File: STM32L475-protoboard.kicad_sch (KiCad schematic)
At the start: 69 parts, among them J1 USB_HEADER, J10 Conn_01x02_Male, J11 SD_Card, J2 USB_B_Micro, J3 DCin, J4 STLINK, J5 W5500_ETHERNET, J6 STLINK2, J7 BOOT_MODE, J8 Conn_02x20_Odd_Even, J9 Conn_01x02_Male, SW1 RESET, U1 SRV05-4, U2 AMS1117-3.3, U3 STM32L475RCTx, Y1 16 MHz, Y2 32.768k

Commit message: some more pins
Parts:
- added C20, C21: 12p, Capacitor_SMD:C_0603_1608Metric, symbol Device:C_Small
- added J10: GNDPAD, Connector_Wire:SolderWirePad_1x01_SMD_1x2mm, symbol Connector:Conn_01x01_Male
- added J8: PAD_PA9_USART1_TX, Connector_Wire:SolderWirePad_1x01_SMD_1x2mm, symbol Connector:Conn_01x01_Male
- added J9: PAD_PA10_USART1_RX, Connector_Wire:SolderWirePad_1x01_SMD_1x2mm, symbol Connector:Conn_01x01_Male
- renumbered C11 to C10, C12 to C11, C13 to C12, C7 to C13, C19 to C18, C18 to C19, C20 to C22, C21 to C23, C22 to C24, C8 to C7, C9 to C8, C10 to C9, J9 to J11, J10 to J12, J8 to J13, J11 to J14, R3 to R2, R4 to R3, R5 to R4, R6 to R5, R2 to R6
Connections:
- net +3V3: now also J13.7 (Pin_7)
- net GND: now also C20.1, C21.1, J10.1 (Pin_1)
- net LED_USR1: now also J13.39 (Pin_39); no longer J13.37 (Pin_37)
- net LED_USR2: now also J13.37 (Pin_37); no longer J13.39 (Pin_39)
- net PA2: now reaches U3.16 (PA2)
- net PA2: now also J13.35 (Pin_35)
- net PA3: now reaches U3.17 (PA3)
- net PA3: now also J13.33 (Pin_33)
- net PA4: now reaches U3.20 (PA4)
- net PA4: now also J13.31 (Pin_31)
- net PA5: now reaches U3.21 (PA5)
- net PA5: now also J13.29 (Pin_29)
- net PA6: now reaches U3.22 (PA6)
- net PA6: now also J13.27 (Pin_27), C20.2
- net PA7: now reaches U3.23 (PA7)
- net PA7: now also J13.25 (Pin_25), C21.2
- net PA9: now reaches U3.42 (PA9)
- net PA9: now also J8.1 (Pin_1)
- net USB_ID renamed PA10
- net PA10: now also J9.1 (Pin_1)
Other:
- moved on the sheet: J13

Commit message: texts
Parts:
- C20, C21: value 12p -> DNP; footprint Capacitor_SMD:C_0603_1608Metric -> Capacitor_SMD:C_0805_2012Metric_Pad1.18x1.45mm_HandSolder
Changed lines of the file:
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@@
     (in_bom yes) (on_board yes)
     (property "Reference" "C21" (id 0) (at 231.14 62.23 90))
-    (property "Value" "12p" (id 1) (at 233.68 62.23 90))
-    (property "Footprint" "Capacitor_SMD:C_0603_1608Metric" (id 2) (at 228.6 62.23 0)
+    (property "Value" "DNP" (id 1) (at 233.68 62.23 90))
+    (property "Footprint" "Capacitor_SMD:C_0805_2012Metric_Pad1.18x1.45mm_HandSolder" (id 2) (at 228.6 62.23 0)
       (effects (font (size 1.27 1.27)) hide)
     )
@@
     (in_bom yes) (on_board yes)
     (property "Reference" "C20" (id 0) (at 231.14 52.07 90))
-    (property "Value" "12p" (id 1) (at 233.68 52.07 90))
-    (property "Footprint" "Capacitor_SMD:C_0603_1608Metric" (id 2) (at 228.6 52.07 0)
+    (property "Value" "DNP" (id 1) (at 233.68 52.07 90))
+    (property "Footprint" "Capacitor_SMD:C_0805_2012Metric_Pad1.18x1.45mm_HandSolder" (id 2) (at 228.6 52.07 0)
       (effects (font (size 1.27 1.27)) hide)
     )
@@
     )
     (path "/e06a59e6-3afe-4857-8998-a5946749a3af"
-      (reference "C20") (unit 1) (value "12p") (footprint "Capacitor_SMD:C_0603_1608Metric")
+      (reference "C20") (unit 1) (value "DNP") (footprint "Capacitor_SMD:C_0805_2012Metric_Pad1.18x1.45mm_HandSolder")
     )
     (path "/097e26fe-f01a-4812-ac65-b308a8eb46ac"
-      (reference "C21") (unit 1) (value "12p") (footprint "Capacitor_SMD:C_0603_1608Metric")
+      (reference "C21") (unit 1) (value "DNP") (footprint "Capacitor_SMD:C_0805_2012Metric_Pad1.18x1.45mm_HandSolder")
     )
     (path "/bf7728b2-c0d3-4e01-ba3c-30550cdcc695"

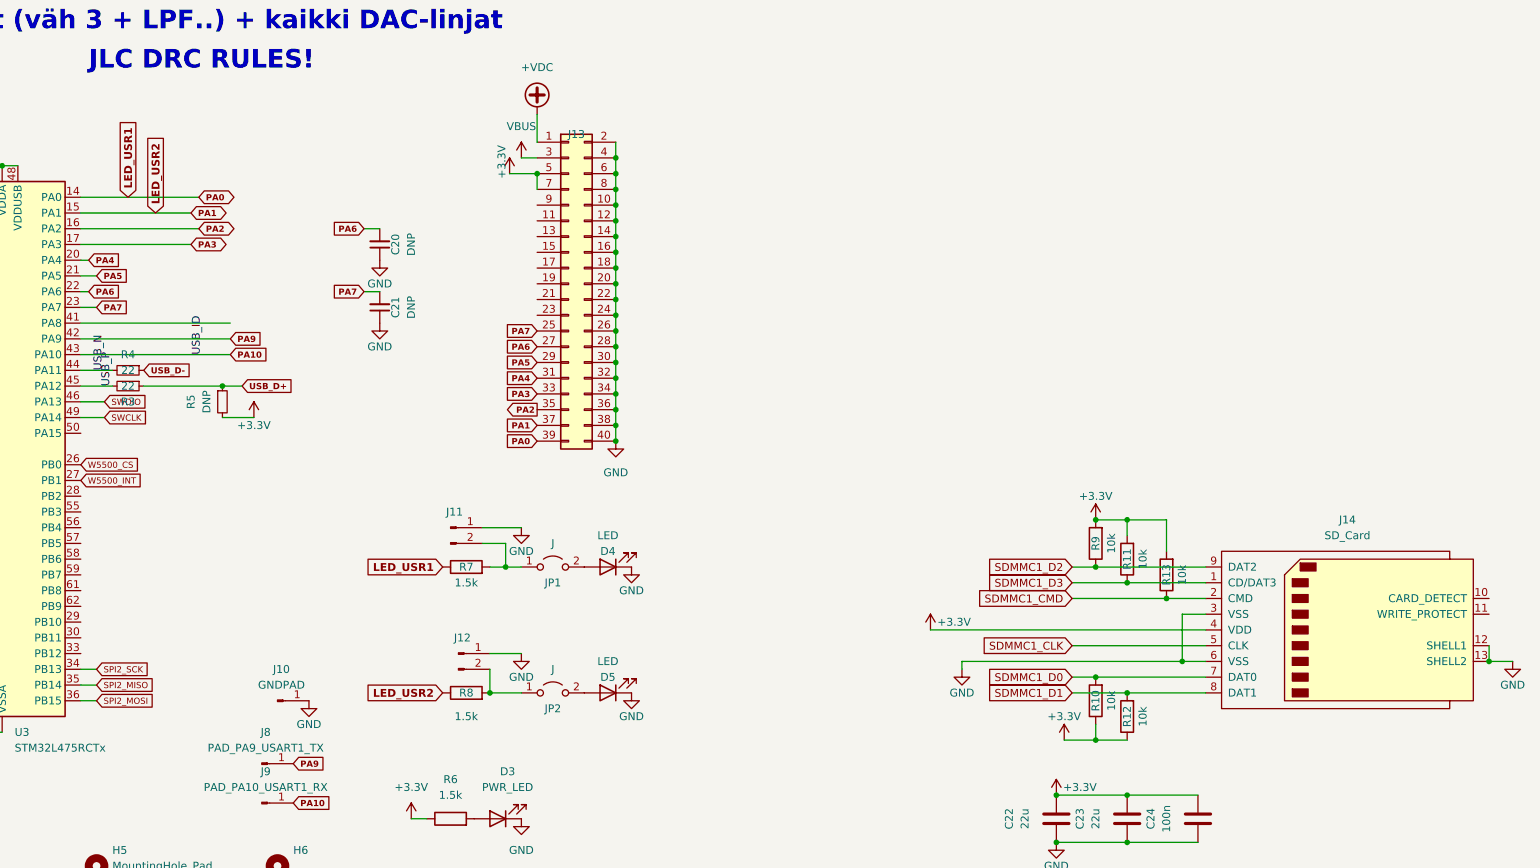
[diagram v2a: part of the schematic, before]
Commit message: SD -> microSD, w.i.p
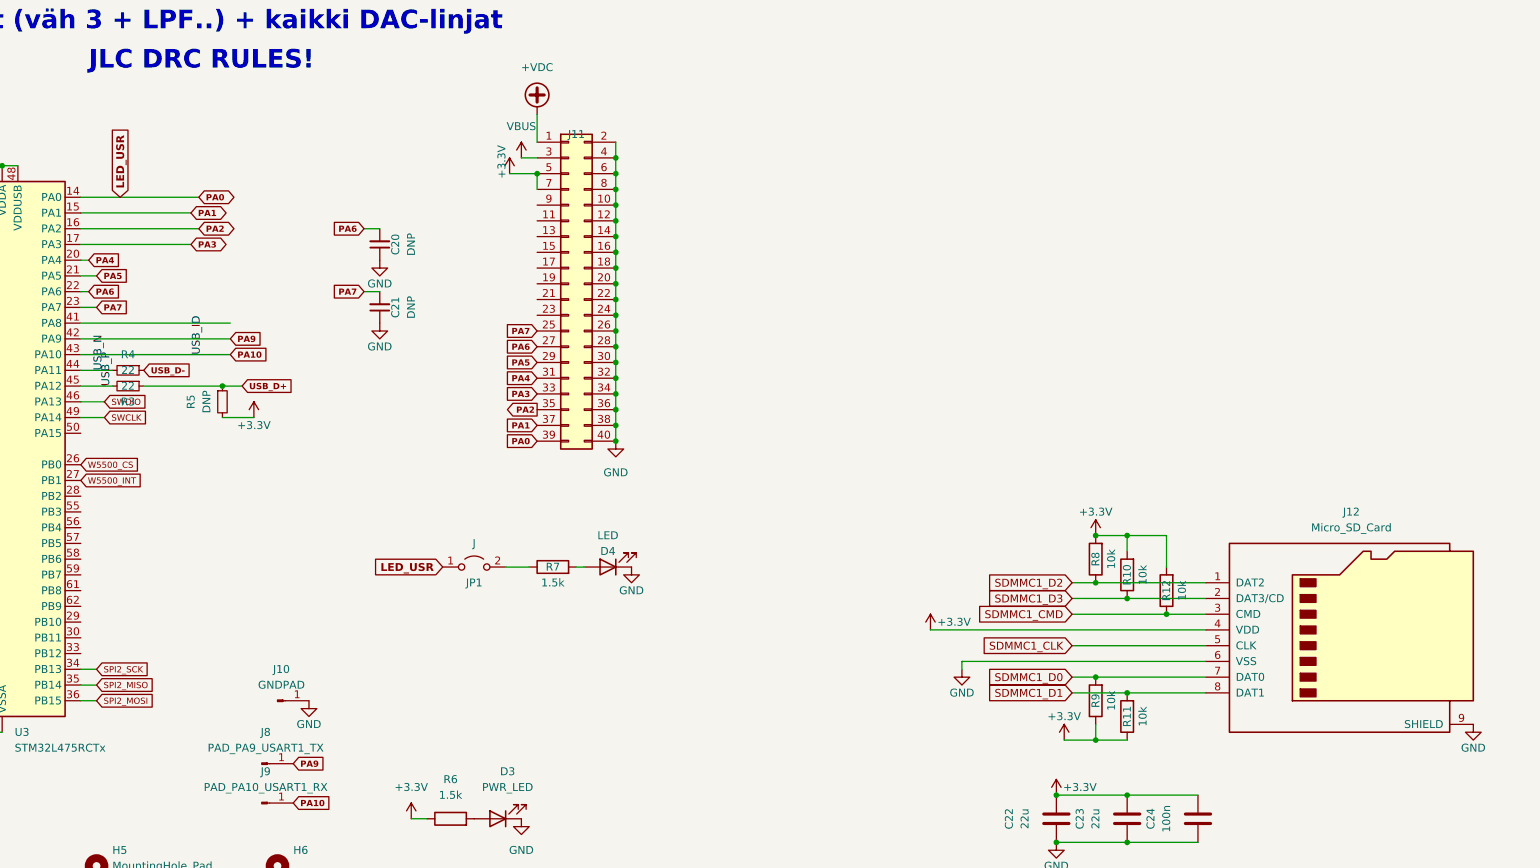
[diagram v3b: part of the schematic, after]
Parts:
- removed D5: LED, LED_SMD:LED_0805_2012Metric, symbol Device:LED
- removed J11, J12: Conn_01x02_Male, Connector_PinHeader_2.54mm:PinHeader_1x02_P2.54mm_Vertical, symbol Connector:Conn_01x02_Male
- removed J14: SD_Card, Connector_Card:SD_Kyocera_145638109211859+, symbol Connector:SD_Card
- removed JP2: J, Jumper:SolderJumper-2_P1.3mm_Open_RoundedPad1.0x1.5mm, symbol Jumper:Jumper_2_Open
- removed R8: 1.5k, Resistor_SMD:R_0603_1608Metric_Pad0.98x0.95mm_HandSolder, symbol Device:R
- added J12: Micro_SD_Card, Connector_Card:microSD_HC_Wuerth_693072010801, symbol Connector:Micro_SD_Card
- renumbered J13 to J11, R11 to R10, R12 to R11, R13 to R12, R9 to R8, R10 to R9
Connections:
- net +3V3: now also J12.4 (VDD)
- net GND: now also J12.6 (VSS), J12.9 (SHIELD)
- net SDMMC1_CLK: now also J12.5 (CLK)
- net SDMMC1_CMD: now also J12.3 (CMD)
- net SDMMC1_D0: now also J12.7 (DAT0)
- net SDMMC1_D1: now also J12.8 (DAT1)
- net SDMMC1_D2: now also J12.1 (DAT2)
- net SDMMC1_D3: now also J12.2 (DAT3/CD)
- net at R7.2: now also D4.2 (A); no longer JP1.1 (A)
- net at JP1.2 (B): now also R7.1; no longer D4.2 (A)
- net LED_USR1 renamed LED_USR
- net LED_USR: now also JP1.1 (A); no longer R7.1
- net LED_USR2 renamed PA1
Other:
- moved on the sheet: JP1, R10, R12, R7, R8

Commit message: todo: find proper microSD connector from JLC
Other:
- note added: "TODO: A/D:lle lowpass"
- note removed: "TODO: A/D:lle lowpass-optio, oletuksena 0R-vastus"
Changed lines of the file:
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@@
     (effects (font (size 1.27 1.27)) (justify left bottom))
   )
-  (text "TODO: A/D:lle lowpass-optio, \noletuksena 0R-vastus"
-    (at 72.39 24.13 0)
+  (text "TODO: A/D:lle lowpass" (at 72.39 24.13 0)
     (effects (font (size 3 3) (thickness 0.6) bold) (justify left bottom))
   )

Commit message: moved mcu a littlebit left
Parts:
- added R1, R4: 330, Resistor_SMD:R_0603_1608Metric_Pad0.98x0.95mm_HandSolder, symbol Device:R
- renumbered R8 to R10, R9 to R11, R10 to R12, R11 to R13, R12 to R14, R1 to R2, R2 to R3, R3 to R5, R4 to R6, R5 to R7, R6 to R8, R7 to R9
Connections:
- net SPI2_MISO: now also R1.2; no longer J5.3 (Pin_3)
- net SPI2_MOSI: now also R4.2; no longer U3.36 (PB15)
- new net: R4.1, U3.36 (PB15)
- new net: J5.3 (Pin_3), R1.1
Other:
- note added: "-USB ID pin + pull-up datalinjaan -tsekkaa DFU-homma -A/D:t (väh 3 + LPF..) + kaikki DAC-linjat"
- note added: "TSEKKAA myös STM32 VBUS-pinni"
- note removed: "MISO/MOSI-VASTUKSET?"
- note removed: "USB ID pin + pull-up datalinjaan tsekkaa DFU-homma A/D:t (väh 3 + LPF..) + kaikki DAC-linjat"
- note removed: "USB_OTG_FS_ID!!! TSEKKAA myös STM32 VBUS-pinni"
- moved on the sheet: C1, C10, C16, C17, C20, C21, C22, C23, C24, C3, C4, C5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

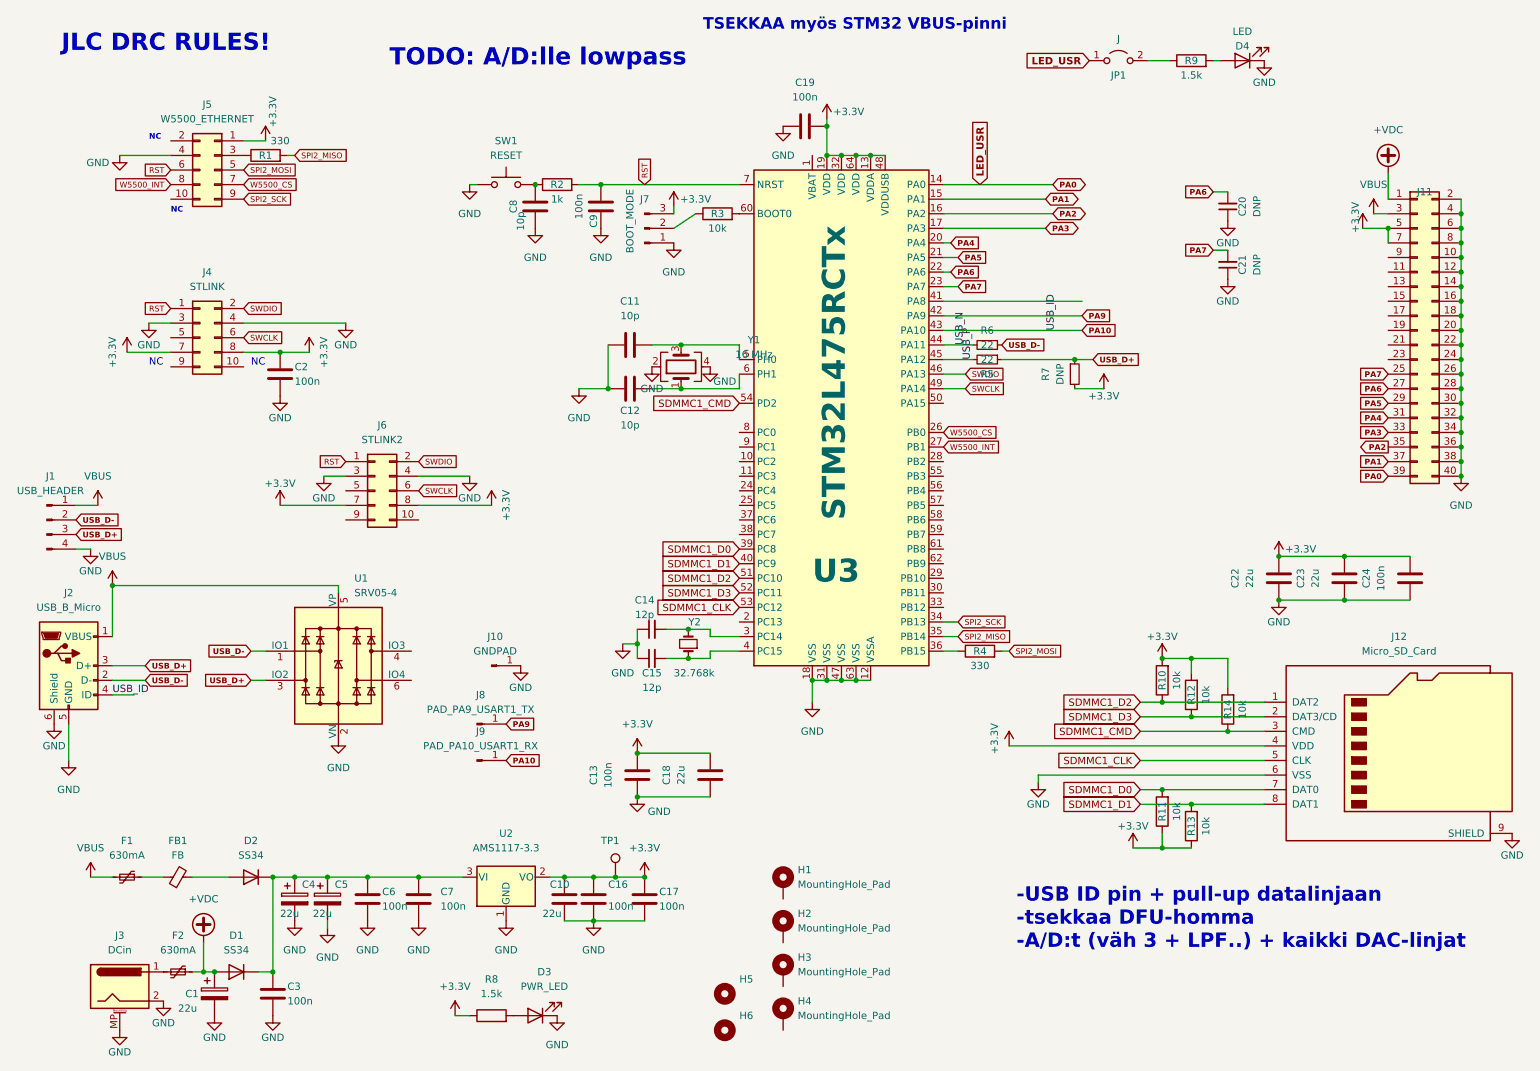
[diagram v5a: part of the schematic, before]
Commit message: migration to KiCAD7
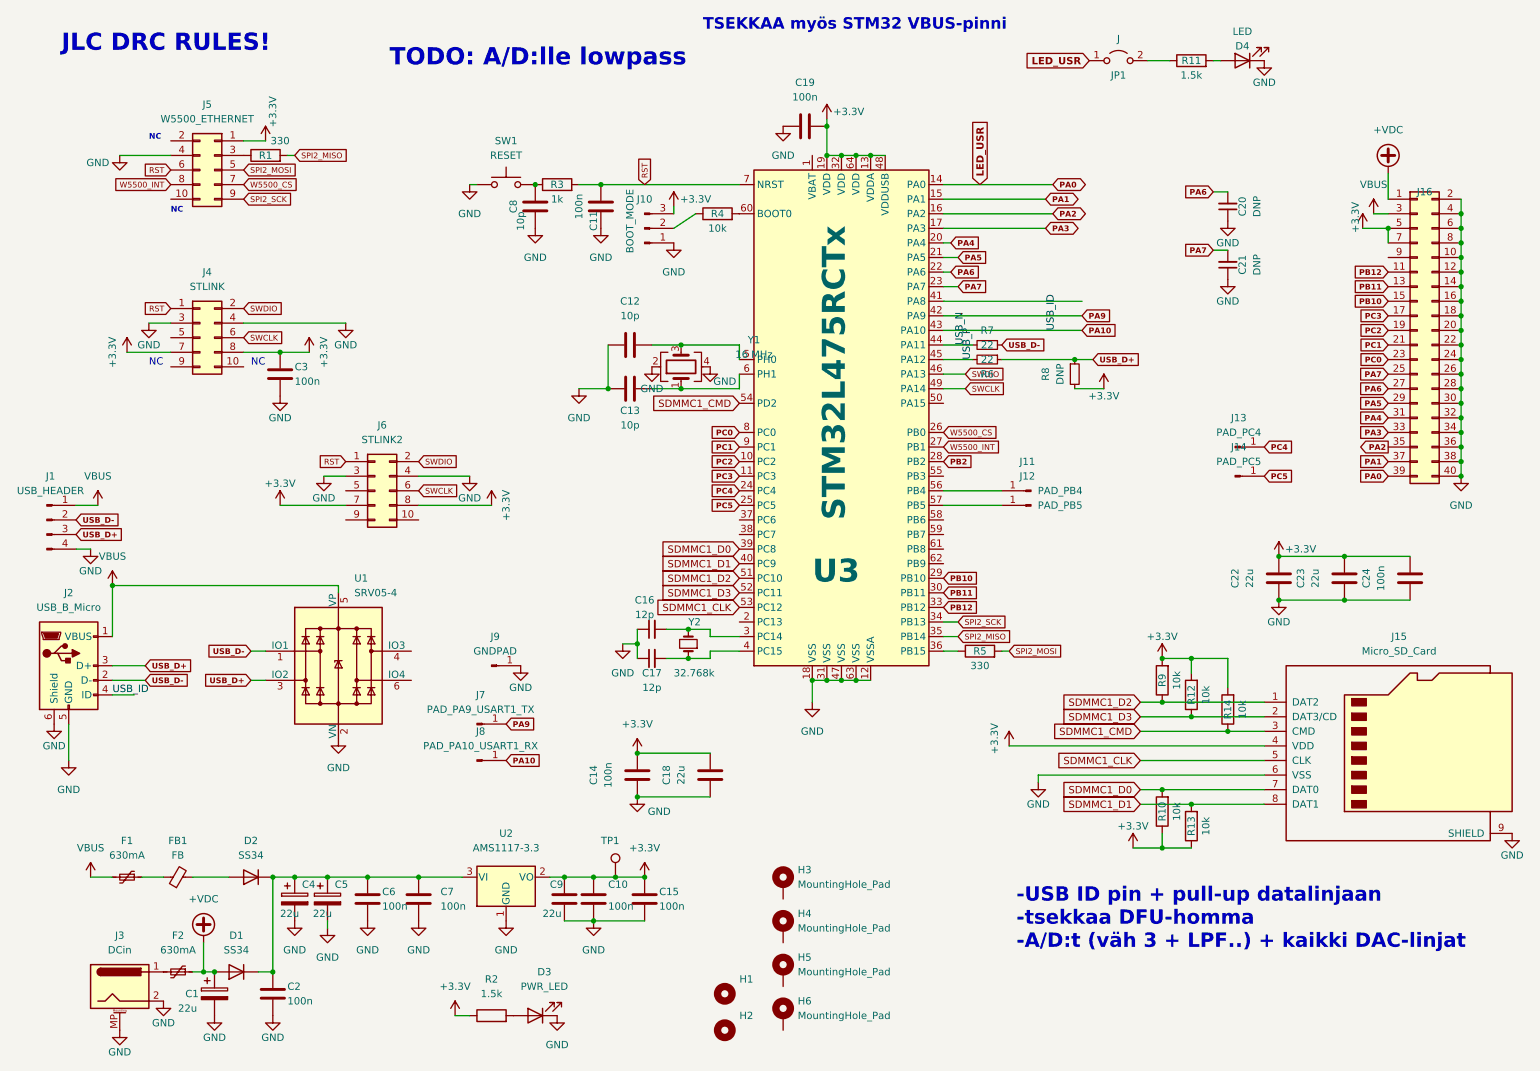
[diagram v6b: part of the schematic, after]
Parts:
- added J11: PAD_PB4, Connector_Wire:SolderWirePad_1x01_SMD_1x2mm, symbol Connector:Conn_01x01_Male
- added J12: PAD_PB5, Connector_Wire:SolderWirePad_1x01_SMD_1x2mm, symbol Connector:Conn_01x01_Male
- added J13: PAD_PC4, Connector_Wire:SolderWirePad_1x01_SMD_1x2mm, symbol Connector:Conn_01x01_Male
- added J14: PAD_PC5, Connector_Wire:SolderWirePad_1x01_SMD_1x2mm, symbol Connector:Conn_01x01_Male
- renumbered C16 to C10, C9 to C11, C11 to C12, C12 to C13, C13 to C14, C17 to C15, C14 to C16, C15 to C17, C3 to C2, C2 to C3, C10 to C9, H5 to H1, H6 to H2, H1 to H3, H2 to H4, H3 to H5, H4 to H6, J7 to J10, J12 to J15, J11 to J16, J8 to J7, J9 to J8, J10 to J9, R11 to R10, R9 to R11, R8 to R2, R2 to R3, R3 to R4, R4 to R5, R5 to R6, R6 to R7, R7 to R8, R10 to R9
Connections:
- net PC2: now reaches U3.10 (PC2)
- net PC2: now also J16.19 (Pin_19)
- net PC3: now reaches U3.11 (PC3)
- net PC3: now also J16.17 (Pin_17)
- net PC4: now reaches U3.24 (PC4)
- net PC4: now also J13.1 (Pin_1)
- net PC5: now reaches U3.25 (PC5)
- net PC5: now also J14.1 (Pin_1)
- net PB2: now reaches U3.28 (PB2)
- net PB10: now reaches U3.29 (PB10)
- net PB10: now also J16.15 (Pin_15)
- net PB11: now reaches U3.30 (PB11)
- net PB11: now also J16.13 (Pin_13)
- net PB12: now reaches U3.33 (PB12)
- net PB12: now also J16.11 (Pin_11)
- net at U3.56 (PB4): now also J11.1 (Pin_1)
- net at U3.57 (PB5): now also J12.1 (Pin_1)
- net PC0: now reaches U3.8 (PC0)
- net PC0: now also J16.23 (Pin_23)
- net PC1: now reaches U3.9 (PC1)
- net PC1: now also J16.21 (Pin_21)

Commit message: microsd + misc
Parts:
- removed J15: Micro_SD_Card, Connector_Card:microSD_HC_Wuerth_693072010801, symbol Connector:Micro_SD_Card
- added Card2: TF PUSH, STM32L475-protoboard:TF-SMD_TF-PUSH, symbol easyeda2kicad:TFPUSH
- added D5: LED, LED_SMD:LED_0805_2012Metric, symbol Device:LED
- added J15: PAD_GND, Connector_Wire:SolderWirePad_1x01_SMD_1x2mm, symbol Connector:Conn_01x01_Male
- added R15: 1.5k, Resistor_SMD:R_0603_1608Metric_Pad0.98x0.95mm_HandSolder, symbol Device:R
- added R16: 0, Resistor_SMD:R_0603_1608Metric_Pad0.98x0.95mm_HandSolder, symbol Device:R
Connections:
- net +3V3: now also Card2.4 (VDD), R16.1
- net GND: now also Card2.10, Card2.11, Card2.12, Card2.13, Card2.6 (VSS), D5.1 (K), J15.1 (Pin_1)
- net SDMMC1_CLK: now also Card2.5 (CLX)
- net SDMMC1_CMD: now also Card2.3 (CMD)
- net SDMMC1_D0: now also Card2.7 (DAT0)
- net SDMMC1_D1: now also Card2.8 (DAT1)
- net SDMMC1_D2: now also Card2.1 (DAT2)
- net SDMMC1_D3: now also Card2.2 (CD/DAT3)
- net at U3.1 (VBAT): now also R16.2
- net at U3.58 (PB6): now also R15.1
- net SD_CD: now reaches U3.59 (PB7)
- net SD_CD: now also Card2.9 (CD)
- new net: D5.2 (A), R15.2
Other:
- note added: "I2C 2k2-pullupeilla"
- note removed: "TODO: A/D:lle lowpass"
- note removed: "TSEKKAA myös STM32 VBUS-pinni"
- moved on the sheet: C19

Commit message: to be continued next time
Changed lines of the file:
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@@
   )
   (text "-USB ID pin + pull-up datalinjaan \n-tsekkaa DFU-homma\n-A/D:t (väh 3 + LPF..) + kaikki DAC-linjat\n"
-    (at 193.04 177.8 0)
+    (at 97.79 13.97 0)
     (effects (font (size 2.5 2.5) (thickness 0.6) bold) (justify left bottom))
   )
